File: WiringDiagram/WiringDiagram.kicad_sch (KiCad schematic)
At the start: 58 parts, among them J1 Conn_01x06, J10 Conn_01x04, J11 Conn_01x04, J12 Conn_01x04, J2 Conn_01x02, J3 Conn_01x04, J4 Conn_01x04, J5 Conn_01x06, J6 Conn_01x08, J7 Conn_01x04, J8 Conn_01x04, J9 Conn_01x04, SW1 TELEMETRUM ROTARY SWITCH, SW2 ERS SENDER ROTARY SWITCH, SW3 CAMERA BOARD ROTARY SWITCH, SW4 PERFECTFLITE FLIGHT COMPUTER

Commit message: Fix double connector label
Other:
- note removed: ""K""
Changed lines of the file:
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@@
+		)
+	)
+	(text "\"6\""
+		(exclude_from_sim no)
+		(at 194.818 340.614 0)
+		(effects
+			(font
+				(size 1.27 1.27)
+				(thickness 0.254)
+				(bold yes)
+			)
+		)
+	)
+	(text "\"18\""
+		(exclude_from_sim no)
+		(at 231.648 173.228 0)
+		(effects
+			(font
+				(size 1.27 1.27)
+				(thickness 0.254)
+				(bold yes)
+			)
+		)
+	)
+	(text "\"1\""
+		(exclude_from_sim no)
+		(at 283.21 82.804 0)
+		(effects
+			(font
+				(size 1.27 1.27)
+				(thickness 0.254)
+				(bold yes)
+			)
 		)
 	)
 	(text "\"J\""
 		(exclude_from_sim no)
-		(at 426.466 252.984 0)
+		(at 451.612 99.06 0)
+		(effects
+			(font
+				(size 1.27 1.27)
+				(thickness 0.254)
+				(bold yes)
+			)
+		)
+	)
+	(text "\"4\""
+		(exclude_from_sim no)
+		(at 169.418 269.494 0)
+		(effects
+			(font
+				(size 1.27 1.27)
+				(thickness 0.254)
+				(bold yes)
+			)
+		)
+	)
+	(text "\"19\""
+		(exclude_from_sim no)
+		(at 440.944 79.248 0)
+		(effects
+			(font
+				(size 1.27 1.27)
+				(thickness 0.254)
+				(bold yes)
+			)
+		)
+	)
+	(text "\"7\""
+		(exclude_from_sim no)
+		(at 242.316 282.702 0)
+		(effects
+			(font
+				(size 1.27 1.27)
+				(thickness 0.254)
+				(bold yes)
+			)
+		)
+	)
+	(text "\"20\""
+		(exclude_from_sim no)
+		(at 295.656 102.87 0)
+		(effects
+			(font
+				(size 1.27 1.27)
+				(thickness 0.254)
+				(bold yes)
+			)
+		)
+	)
+	(text "\"5\""
+		(exclude_from_sim no)
+		(at 212.598 85.852 0)
+		(effects
+			(font
+				(size 1.27 1.27)
+				(thickness 0.254)
+				(bold yes)
+			)
+		)
+	)
+	(text "DOWN FRONT"
+		(exclude_from_sim no)
+		(at 247.396 143.764 90)
+		(effects
+			(font
+				(size 1.27 1.27)
+				(thickness 0.254)
+				(bold yes)
+			)
+		)
+	)
+	(text "RKT\nRDY"
+		(exclude_from_sim no)
+		(at 159.766 253.746 0)
+		(effects
+			(font
+				(size 1.27 1.27)
+				(thickness 0.254)
+				(bold yes)
+			)
+		)
+	)
+	(text "\"7\""
+		(exclude_from_sim no)
+		(at 229.616 264.668 0)
 		(effects
 			(font
@@
 	(text "\"6\""
 		(exclude_from_sim no)
-		(at 194.818 340.614 0)
-		(effects
-			(font
-				(size 1.27 1.27)
-				(thickness 0.254)
-				(bold yes)
-			)
-		)
-	)
-	(text "\"18\""
-		(exclude_from_sim no)
-		(at 231.648 173.228 0)
-		(effects
-			(font
-				(size 1.27 1.27)
-				(thickness 0.254)
-				(bold yes)
-			)
-		)
-	)
-	(text "\"1\""
-		(exclude_from_sim no)
-		(at 283.21 82.804 0)
+		(at 229.108 73.66 0)
+		(effects
+			(font
+				(size 1.27 1.27)
+				(thickness 0.254)
+				(bold yes)
+			)
+		)
+	)
+	(text "ERS v4 #???"
+		(exclude_from_sim no)
+		(at 204.47 299.72 0)
 		(effects
 			(font
@@
 	(text "\"4\""
 		(exclude_from_sim no)
-		(at 169.418 269.494 0)
-		(effects
-			(font
-				(size 1.27 1.27)
-				(thickness 0.254)
-				(bold yes)
-			)
-		)
-	)
-	(text "\"19\""
-		(exclude_from_sim no)
-		(at 440.944 79.248 0)
-		(effects
-			(font
-				(size 1.27 1.27)
-				(thickness 0.254)
-				(bold yes)
-			)
-		)
-	)
-	(text "\"7\""
-		(exclude_from_sim no)
-		(at 242.316 282.702 0)
-		(effects
-			(font
-				(size 1.27 1.27)
-				(thickness 0.254)
-				(bold yes)
-			)
-		)
-	)
-	(text "\"20\""
-		(exclude_from_sim no)
-		(at 295.656 102.87 0)
-		(effects
-			(font
-				(size 1.27 1.27)
-				(thickness 0.254)
-				(bold yes)
-			)
-		)
-	)
-	(text "\"5\""
-		(exclude_from_sim no)
-		(at 212.598 85.852 0)
-		(effects
-			(font
-				(size 1.27 1.27)
-				(thickness 0.254)
-				(bold yes)
-			)
-		)
-	)
-	(text "DOWN FRONT"
-		(exclude_from_sim no)
-		(at 247.396 143.764 90)
-		(effects
-			(font
-				(size 1.27 1.27)
-				(thickness 0.254)
-				(bold yes)
-			)
-		)
-	)
-	(text "RKT\nRDY"
-		(exclude_from_sim no)
-		(at 159.766 253.746 0)
-		(effects
-			(font
-				(size 1.27 1.27)
-				(thickness 0.254)
-				(bold yes)
-			)
-		)
-	)
-	(text "\"7\""
-		(exclude_from_sim no)
-		(at 229.616 264.668 0)
-		(effects
-			(font
-				(size 1.27 1.27)
-				(thickness 0.254)
-				(bold yes)
-			)
-		)
-	)
-	(text "\"6\""
-		(exclude_from_sim no)
-		(at 229.108 73.66 0)
-		(effects
-			(font
-				(size 1.27 1.27)
-				(thickness 0.254)
-				(bold yes)
-			)
-		)
-	)
-	(text "ERS v4 #???"
-		(exclude_from_sim no)
-		(at 204.47 299.72 0)
-		(effects
-			(font
-				(size 1.27 1.27)
-				(thickness 0.254)
-				(bold yes)
-			)
-		)
-	)
-	(text "\"4\""
-		(exclude_from_sim no)
 		(at 177.038 336.042 0)
 		(effects
@@
 		(exclude_from_sim no)
 		(at 197.358 242.824 0)
+		(effects
+			(font
+				(size 1.27 1.27)
+				(thickness 0.254)
+				(bold yes)
+			)
+		)
+	)
+	(text "\"J\""
+		(exclude_from_sim no)
+		(at 455.93 99.06 0)
 		(effects
 			(font
@@
 		)
 	)
-	(text "\"K\""
-		(exclude_from_sim no)
-		(at 451.358 100.076 0)
-		(effects
-			(font
-				(size 1.27 1.27)
-				(thickness 0.254)
-				(bold yes)
-			)
-		)
-	)
 	(text "\"20\""
 		(exclude_from_sim no)
@@
 		)
 	)
-	(text "\"J\""
-		(exclude_from_sim no)
-		(at 426.72 247.65 0)
-		(effects
-			(font
-				(size 1.27 1.27)
-				(thickness 0.254)
-				(bold yes)
-			)
-		)
-	)
 	(text "\"19\""
 		(exclude_from_sim no)
@@
 		(effects
 			(font
-				(size 1.27 1.27)
-				(thickness 0.254)
-				(bold yes)
-			)
-		)
-	)
-	(text "\"K\""
-		(exclude_from_sim no)
-		(at 455.93 100.076 0)
-		(effects
-			(font

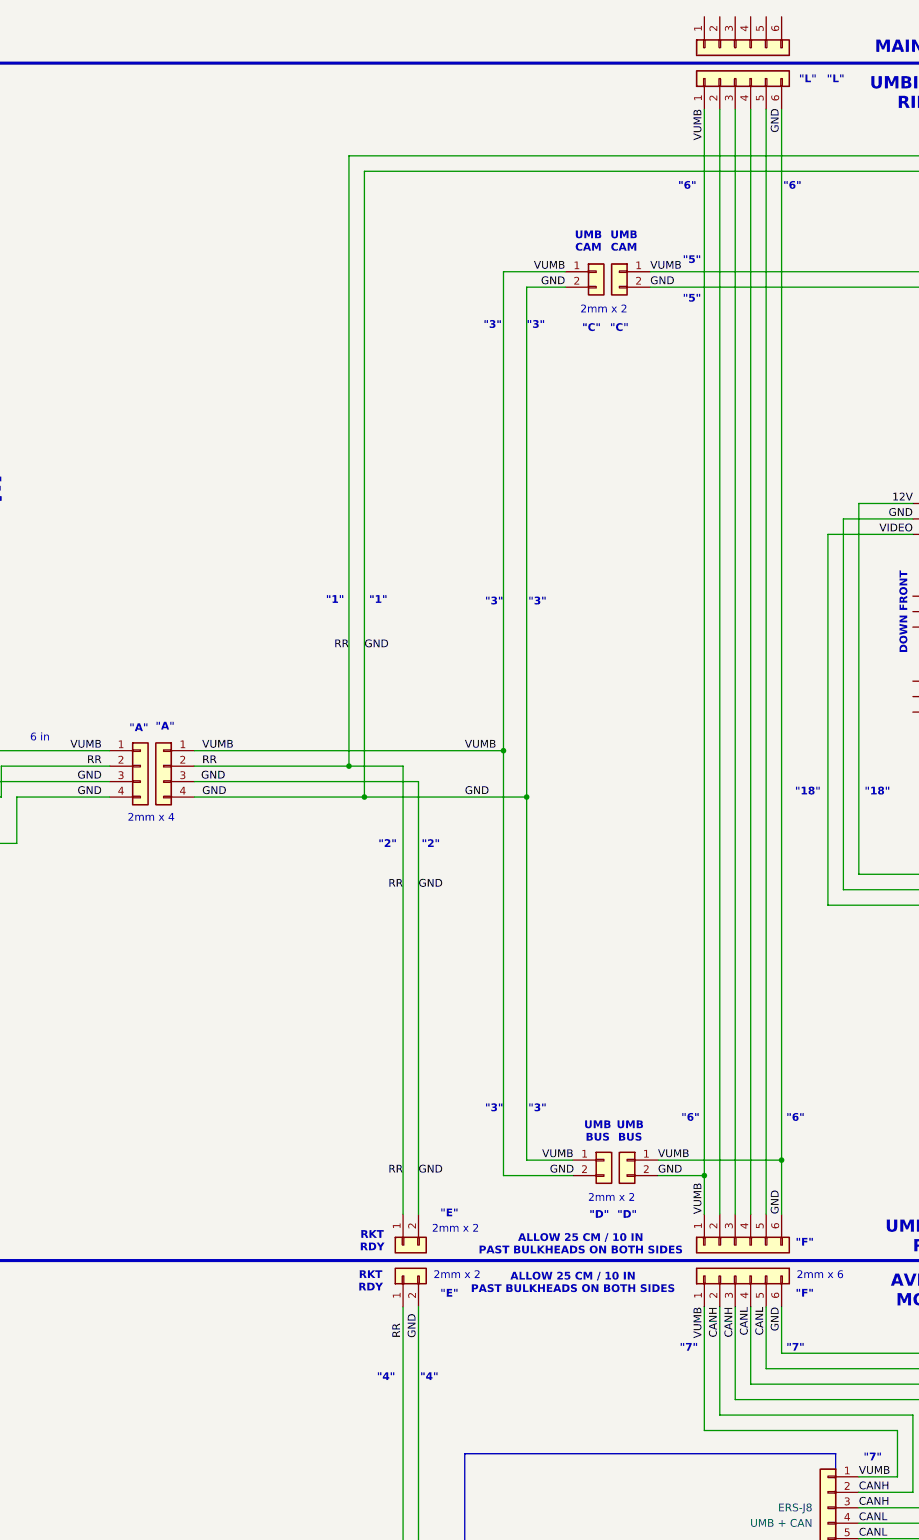
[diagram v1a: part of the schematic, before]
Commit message: Move UMB Bus Connection through the avionics module side
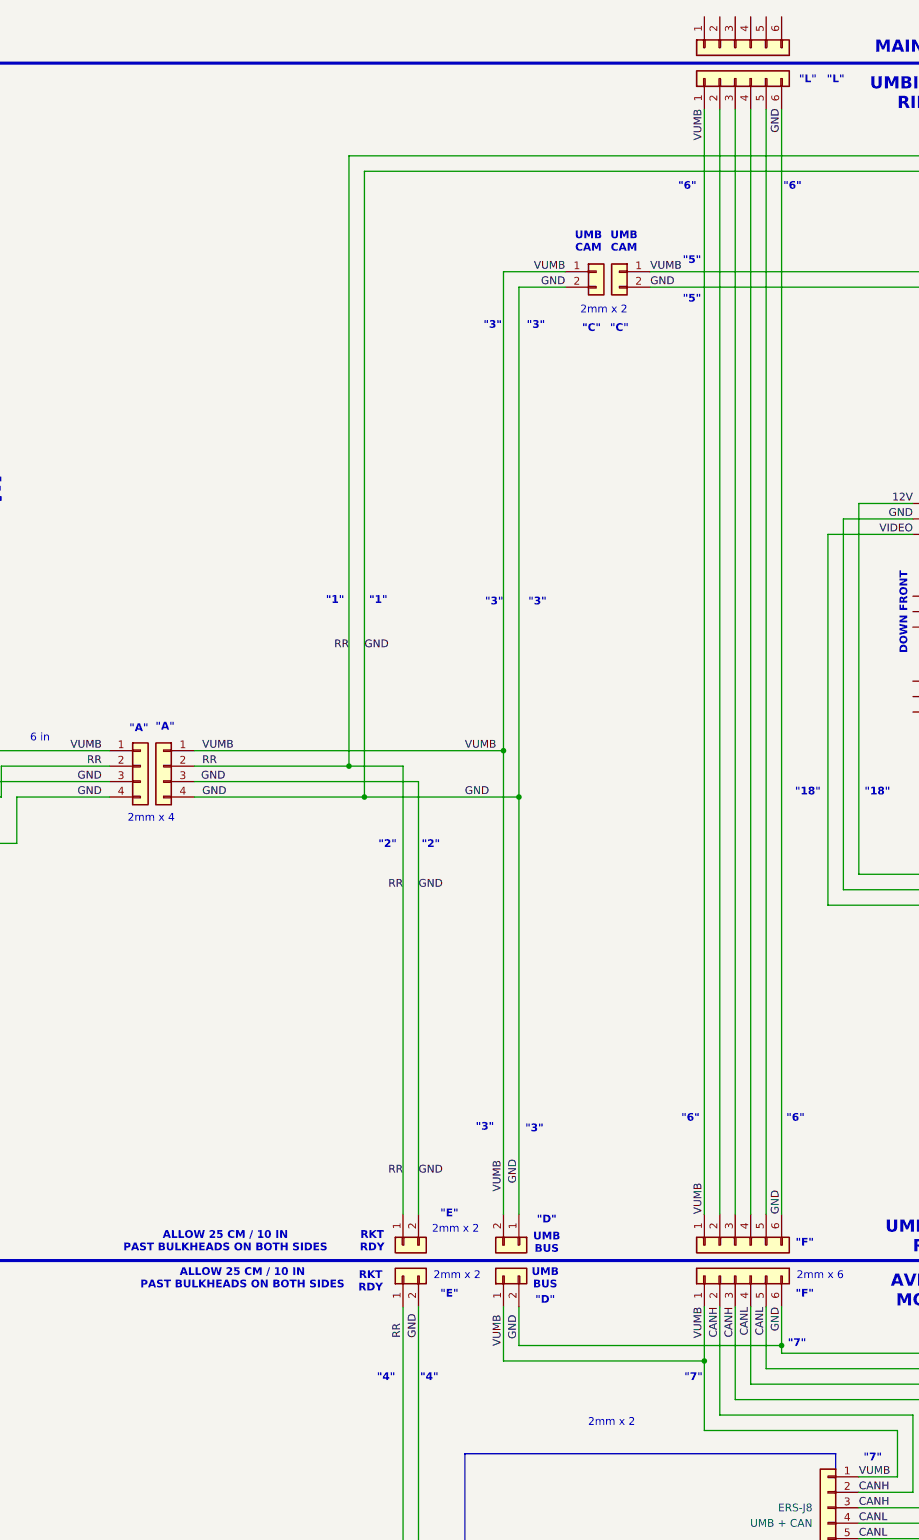
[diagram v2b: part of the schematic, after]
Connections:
- net GND: no longer CAM-JP3.2 (Pin_2), ERS-J18.1 (Pin_1), ERS-J25.2 (Pin_2), ERS-J28.1 (Pin_1), ERS-J29.1 (Pin_1), ERS-J30.1 (Pin_1), ERS-J6.1 (Pin_1), ERS-J7.1 (Pin_1), ERS-J8.1 (Pin_1), J6.1 (Pin_1), J7.1 (Pin_1), J9.1 (Pin_1)
- new net VUMB: CAM-JP3.2 (Pin_2), ERS-J18.1 (Pin_1), ERS-J25.2 (Pin_2), ERS-J28.1 (Pin_1), ERS-J29.1 (Pin_1), ERS-J30.1 (Pin_1), ERS-J6.1 (Pin_1), ERS-J7.1 (Pin_1), ERS-J8.1 (Pin_1), J6.1 (Pin_1), J7.1 (Pin_1), J9.1 (Pin_1)
